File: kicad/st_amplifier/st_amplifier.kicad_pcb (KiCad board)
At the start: 2 copper layers, 170 x 90 mm, 71 parts

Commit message: Adding board st_amplifier.
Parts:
- moved DA1 113.8 mm to (148.6, 120.7)
- moved C1 109.8 mm to (128.9, 120.0), turned to 90 degrees
- moved C2 108.8 mm to (156.8, 119.4)
- moved C3 107.3 mm to (162.6, 120.7)
- moved R5 104.8 mm to (102.2, 74.9)
- moved XS2 102.4 mm to (111.8, 124.5)
- moved R10 99.3 mm to (106.7, 101.6)
- moved VD1 97.5 mm to (111.8, 105.4)
- moved C5 96.7 mm to (156.8, 104.8)
- moved R7 96.7 mm to (104.1, 109.2)
- moved R16 96.3 mm to (189.2, 124.5), turned to 0 degrees
- moved C13 96.0 mm to (177.2, 97.2)
- moved R8 95.7 mm to (177.2, 101.6)
- moved C4 95.7 mm to (128.9, 104.1)
- moved R13 95.6 mm to (221.0, 79.4), turned to 90 degrees
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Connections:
- DA5 pad 5: (no net) -> /CLIP_2
- XS2 pad 4: /CLIP_1 -> /CLIP_2
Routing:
- net /+29V: track 0.00 -> 305.4 mm, vias 0 -> 2
- net /-29V: track 0.00 -> 302.8 mm, vias 0 -> 3
- net /GND: track 0.00 -> 235.1 mm
- net /MUTE: track 0.00 -> 207.6 mm, vias 0 -> 2
- net /STBY: track 0.00 -> 158.8 mm, vias 0 -> 6
- net /CLIP_2: track 0.00 -> 146.0 mm, vias 0 -> 4
- net N-000003: track 0.00 -> 86.0 mm
- net /CLIP_1: track 0.00 -> 75.6 mm, vias 0 -> 2
- net N-0000035: track 0.00 -> 67.6 mm
- net /-15V: track 0.00 -> 59.3 mm
- net N-0000030: track 0.00 -> 54.4 mm
- net N-0000017: track 0.00 -> 47.6 mm
- net N-0000011: track 0.00 -> 46.2 mm
- net N-0000027: track 0.00 -> 44.5 mm
- net N-0000025: track 0.00 -> 39.9 mm
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- added copper zone on B.Cu, net /GND
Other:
- board size 170 x 90 mm -> 170 x 80 mm
- rule trace_min: 0.254 -> 0.25
- board text added: "+VCC"
- board text added: "-VCC"
- board text added: "CLIP 1"
- board text added: "CLIP 2"
- board text added: "GND"
- board text added: "IN 1"
- board text added: "IN 2"
- board text added: "OUT 1"
- board text added: "OUT 2"
- board text added: "SB"

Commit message: New commit.
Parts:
- moved R11 23.1 mm to (82.5, 105.4)
- moved R7 21.6 mm to (82.5, 109.2)
- moved VD1 18.8 mm to (93.3, 109.2), turned to 0 degrees
- moved R9 16.8 mm to (100.3, 105.4), turned to 0 degrees
- moved C18 8.62 mm to (103.5, 94.6)
- moved R10 7.43 mm to (109.2, 94.6), turned to 90 degrees
- moved C6 6.87 mm to (158.8, 109.2), turned to 0 degrees
- moved C3 6.35 mm to (158.8, 115.6), turned to 180 degrees
- moved C19 5.44 mm to (102.9, 100.3), turned to 180 degrees
- moved C11 3.56 mm to (118.4, 74.9)
- moved C2 2.69 mm to (158.8, 121.3)
- moved C5 2.29 mm to (158.8, 103.5)
- moved XS2 1.27 mm to (111.8, 125.7)
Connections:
- XS1 pad 1: /+29V -> /-29V
- XS1 pad 2: /GND -> /+29V
- XS1 pad 3: /-29V -> /GND
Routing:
- net /CLIP_2: track 146.0 -> 180.0 mm, vias 4 -> 2
- net /MU/ST: track 19.7 -> 45.4 mm
- net /MUTE: track 207.6 -> 227.8 mm, vias 2 -> 4
- net /STBY: track 158.8 -> 177.0 mm, vias 6 -> 5
- net /GND: track 235.1 -> 219.4 mm
- net /-29V: track 302.8 -> 316.9 mm
- net /+29V: track 305.4 -> 314.7 mm
- net /-15V: track 59.3 -> 63.4 mm
- net N-0000028: track 14.0 -> 11.4 mm
- net /+15V: track 34.6 -> 36.5 mm
- net N-0000011: track 46.2 -> 44.4 mm
- net N-0000012: track 13.9 -> 12.2 mm
- net N-0000026: track 27.4 -> 28.8 mm
- net N-0000025: track 39.9 -> 38.4 mm
- net /CLIP_1: track 75.6 -> 74.2 mm
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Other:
- net class Default: clearance 0.254 -> 0.35; trace_width 0.254 -> 0.5
- rule trace_clearance: 0.254 -> 0.35
- rule trace_min: 0.25 -> 0.35

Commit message: New commit.
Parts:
- added R21: 220, RESISTOR_0.25W, F.Cu at (200.0, 99.1)
- added R22: 220, RESISTOR_0.25W, F.Cu at (198.8, 114.9)
- moved C21 8.64 mm to (196.2, 95.2), turned to 0 degrees
- moved R12 5.24 mm to (200.0, 103.5), turned to 0 degrees
- moved C27 4.58 mm to (194.9, 112.4)
- moved R16 4.02 mm to (185.4, 125.7)
- moved R6 4.02 mm to (185.4, 120.0)
- moved C23 1.27 mm to (190.5, 102.9)
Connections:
- C20 pad 2: N-0000034 (its old number) -> N-0000033
- C21 pad 2: N-0000034 (its old number) -> N-0000032
- C24 pad 2: N-000001 -> N-000002
- C27 pad 2: N-000001 -> N-000003
- DA3 pad 3: N-0000034 (its old number) -> N-0000032
- DA3 pad 5: N-000001 -> N-000003
- R12 pad 2: N-0000034 (its old number) -> N-0000033
- R18 pad 2: N-000001 -> N-000002
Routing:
- net N-0000034 (its old number): track 37.7 -> 0.00 mm
- net N-000001: track 28.5 -> 0.00 mm
- net N-0000032: track 0.00 -> 25.2 mm
- net N-000003: track 0.00 -> 18.4 mm
- net N-000002: track 0.00 -> 17.2 mm
- net N-0000033: track 0.00 -> 10.8 mm
- net N-000004: track 26.7 -> 23.8 mm
- net N-0000016: track 48.1 -> 50.9 mm
- net /-15V: track 63.4 -> 62.9 mm

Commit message: New commit.
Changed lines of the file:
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@@
     (area 67.9506 45.9796 241.9294 131.4394)
     (thickness 1.6002)
-    (drawings 30)
+    (drawings 28)
     (tracks 440)
     (zones 0)
@@
       (drillshape 0)
       (scaleselection 1)
-      (outputdirectory ../../../../Документы/GERBER_st_amplifier/))
+      (outputdirectory "/home/vdn/Рабочий стол/st_amplifier_doc/"))
   )
   (net 0 "")
@@
     (effects (font (size 1.7 1.5) (thickness 0.3)))
   )
-  (gr_line (start 135.255 125.73) (end 146.05 125.73) (angle 90) (layer F.SilkS) (width 0.381))
-  (gr_line (start 135.255 115.57) (end 146.05 115.57) (angle 90) (layer F.SilkS) (width 0.381))
   (gr_text GND (at 231.775 111.125) (layer F.SilkS)
     (effects (font (size 1.27 1) (thickness 0.25)))

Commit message: New commit.
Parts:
- removed R21, R22: 220, RESISTOR_0.25W
- added 1_PIN: P***, 1_pin, F.Cu at (145.0, 105.0)
- added 1_PIN: P***, 1_pin, F.Cu at (142.6, 122.2)
- moved C21 3.42 mm to (197.5, 98.4), turned to 180 degrees
- moved R18 3.18 mm to (200.7, 115.6), turned to 270 degrees
- moved R12 0.90 mm to (200.7, 102.9), turned to 180 degrees
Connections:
- C20 pad 2: N-0000033 -> N-0000034
- C21 pad 2: N-0000032 (its old number) -> N-0000034
- C24 pad 2: N-000002 (its old number) -> N-000001
- C27 pad 2: N-000003 (its old number) -> N-000001
- DA3 pad 3: N-0000032 (its old number) -> N-0000034
- DA3 pad 5: N-000003 (its old number) -> N-000001
- R12 pad 2: N-0000033 -> N-0000034
- R18 pad 2: N-000002 (its old number) -> N-000001
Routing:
- net N-0000034: track 0.00 -> 37.5 mm
- net N-000001: track 0.00 -> 27.0 mm
- net N-0000032 (its old number): track 25.2 -> 0.00 mm
- net N-000003 (its old number): track 18.4 -> 0.00 mm
- net N-000002 (its old number): track 17.2 -> 0.00 mm
- net N-0000033: track 10.8 -> 0.00 mm
- net N-0000017: track 50.9 -> 51.9 mm

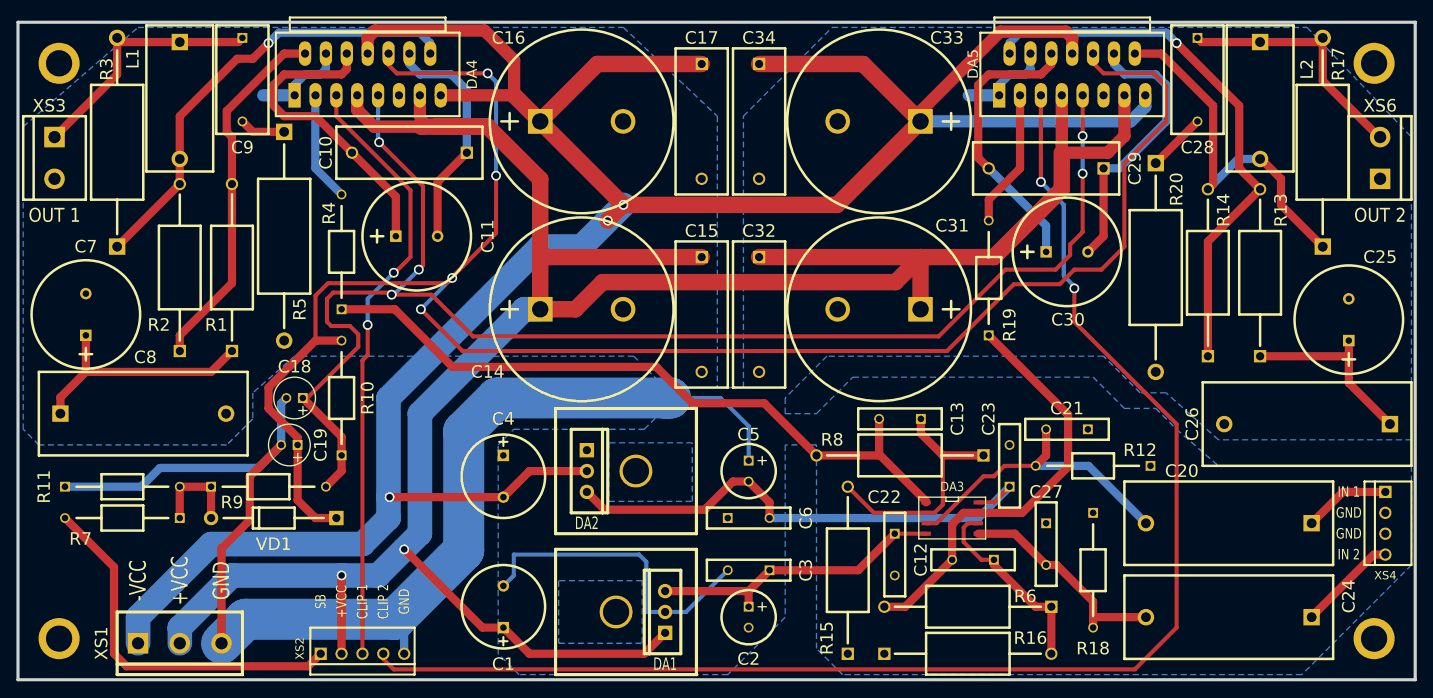
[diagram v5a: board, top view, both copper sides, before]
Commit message: Completely threw PCB board st_amplifier.
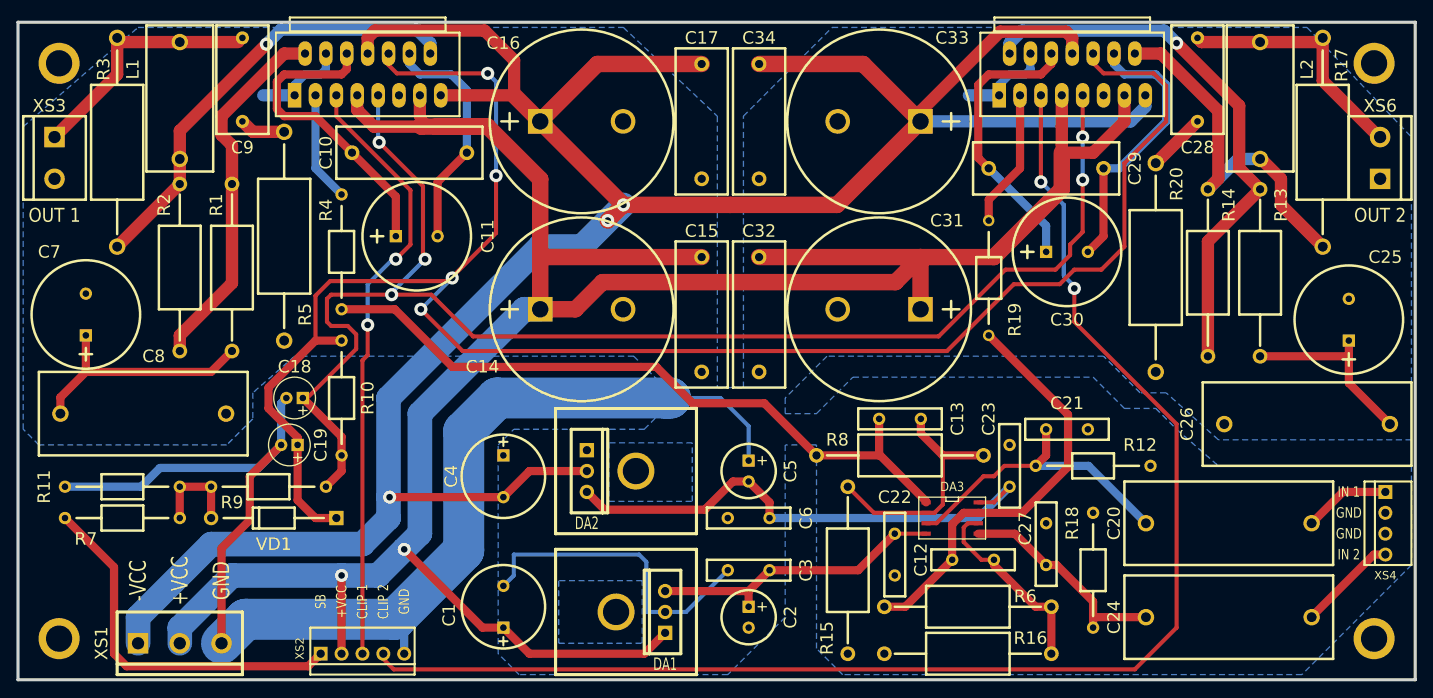
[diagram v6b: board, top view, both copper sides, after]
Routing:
- net /+29V: track 314.6 -> 313.5 mm
- net N-0000030: track 55.5 -> 54.8 mm
- net N-0000036: track 30.7 -> 31.4 mm
- net N-0000011: track 44.4 -> 44.9 mm
- net N-0000027: track 44.5 -> 45.0 mm
- net /STBY: track 177.0 -> 176.5 mm

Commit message: Fixed errors.
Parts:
- R1: value 1 к +/-0.5% -> 2 к +/-0.5%
- R13: value 1 к +/- 0.5% -> 2 к +/-0.5%
- R14: value 2 к +/- 0.5% -> 28.7 к +/-0.5%
- R19, R4: value 2,7 к -> 100
- R2: value 2 к +/-0.5% -> 28.7 к +/-0.5%
- R6, R8: value 47 к +/-0.5% -> 22.1 к +/-0.5%
- moved C33 0.13 mm to (174.5, 61.0), turned to 0 degrees
- turned C16 to 180 degrees
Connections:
- C16 pad 1: /-29V -> /GND
- C16 pad 2: /GND -> /-29V
- C22 pad 1: /+15V -> /-15V
- C23 pad 1: /-15V -> /+15V
- C33 pad 1: /-29V -> /GND
- C33 pad 2: /GND -> /-29V
- DA3 pad 4: /+15V -> /-15V
- DA3 pad 8: /-15V -> /+15V
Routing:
- net /+15V: track 36.5 -> 53.7 mm
- net /-15V: track 62.9 -> 47.3 mm

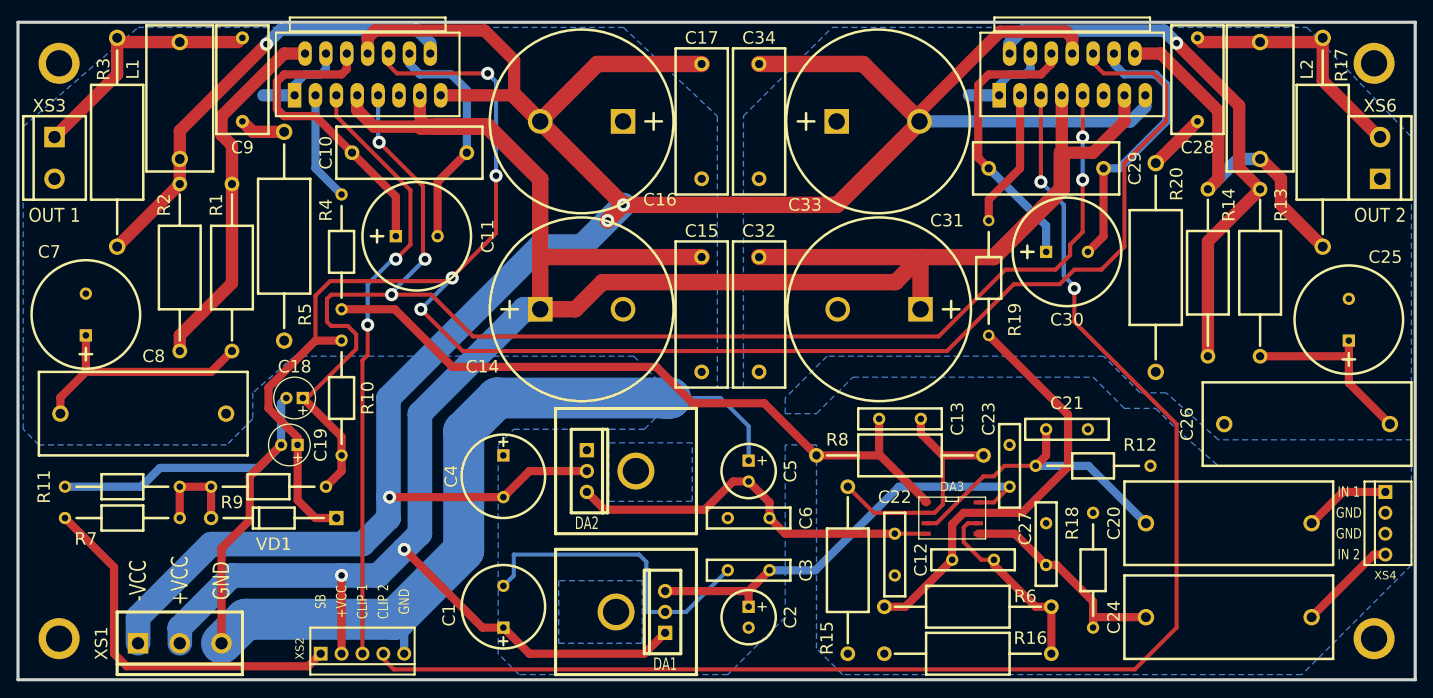
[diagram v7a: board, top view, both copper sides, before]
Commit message: Adding new version st_amplifier.
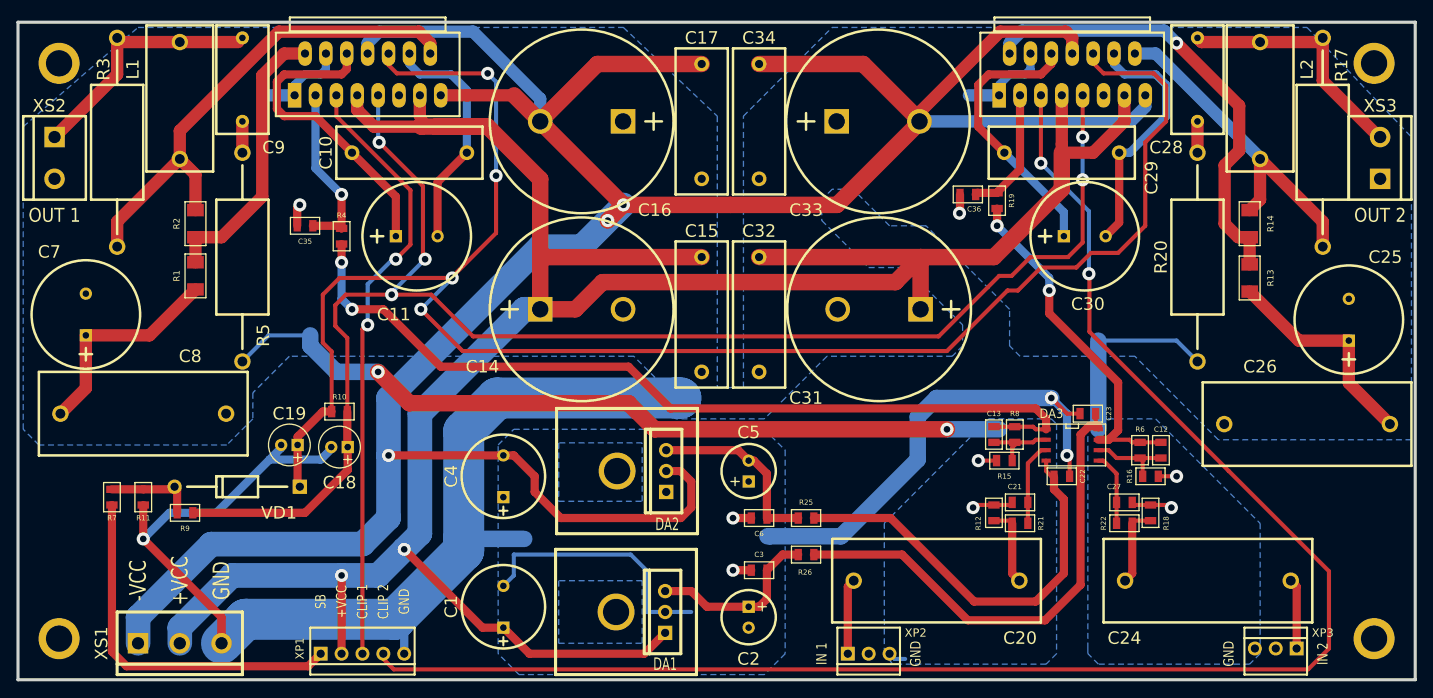
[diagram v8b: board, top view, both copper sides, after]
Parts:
- removed XS4: WF-4, WF-4
- added C35: 22 п, SMD0805, F.Cu at (104.8, 73.7)
- added C36: 22 п, SMD0805, F.Cu at (185.4, 69.8)
- added R21: 220, SMD0805, F.Cu at (191.8, 109.9)
- added R22: 220, SMD0805, F.Cu at (204.5, 109.9)
- added R25: 4.7, SMD0805, F.Cu at (165.7, 109.2)
- added R26: 4.7, SMD0805, F.Cu at (165.7, 113.7)
- added XP2: WF-3, WF-3, F.Cu at (173.4, 125.7)
- added XP3: WF-3, WF-3, F.Cu at (222.9, 125.1)
- C12, C13: value 10 п -> 22 п; footprint CAPACITOR_K10-17 -> SMD0805
- C21, C27: value 100 п -> 220 п; footprint CAPACITOR_K10-17 -> SMD0805
- C22, C23, C3, C6: footprint CAPACITOR_K10-17 -> SMD0805
- C28, C9: value 0.1 мк -> 0.047 мк
- R1: value 2 к +/-0.5% -> 2 к +/-0.5%; footprint RESISTOR_1W -> SMD1206
- R10, R11, R12, R18, R19, R4, R7, R9: footprint RESISTOR_0.25W -> SMD0805
- R13, R14: footprint RESISTOR_1W -> SMD1206
- R15, R16, R6, R8: footprint RESISTOR_1W -> SMD0805
- R2: value 28.7 к +/-0.5% -> 28.7 к +/-0.5%; footprint RESISTOR_1W -> SMD1206
- moved C20 36.2 mm to (181.6, 116.8), turned to 0 degrees
- moved R16 31.0 mm to (207.6, 104.1), turned to 180 degrees
- moved R6 28.3 mm to (206.4, 101.0), turned to 90 degrees
- moved C12 26.5 mm to (208.9, 101.0), turned to 90 degrees
- moved R15 23.3 mm to (189.9, 102.2), turned to 0 degrees
- moved C22 22.4 mm to (196.8, 104.1), turned to 0 degrees
- moved DA3 17.1 mm to (198.1, 100.3)
- moved R8 14.2 mm to (191.1, 99.1), turned to 90 degrees
- moved R12 13.4 mm to (188.6, 108.6), turned to 270 degrees
- moved C13 11.6 mm to (188.6, 99.1), turned to 90 degrees
- moved C23 11.4 mm to (200.0, 96.5), turned to 180 degrees
- moved C27 10.8 mm to (204.5, 107.3), turned to 180 degrees
- moved R9 10.6 mm to (90.2, 108.6)
- moved C21 10.6 mm to (191.8, 107.3), turned to 0 degrees
- moved R18 9.88 mm to (207.6, 108.6)
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- renumbered XS2 to XP1, XS3 to XS2, XS6 to XS3
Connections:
- C20 pad 2: N-0000031 -> N-0000033
- C21 pad 2: N-0000031 -> N-0000032
- C22 pad 1: /-15V -> N-0000019
- C23 pad 1: /+15V -> N-0000018
- C24 pad 2: N-000002 -> N-000001
- C27 pad 2: N-000002 -> N-000004
- DA3 pad 3: N-0000031 -> N-0000032
- DA3 pad 4: /-15V -> N-0000019
- DA3 pad 5: N-000002 -> N-000004
- DA3 pad 8: /+15V -> N-0000018
- R12 pad 2: N-0000031 -> N-0000033
- R18 pad 2: N-000002 -> N-000001
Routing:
- net /GND: track 219.4 -> 403.2 mm, vias 0 -> 13
- net N-0000018: track 0.00 -> 60.8 mm
- net N-0000019: track 0.00 -> 50.8 mm
- net N-0000031: track 37.5 -> 0.00 mm
- net /+15V: track 53.7 -> 21.7 mm
- net N-000002: track 27.0 -> 0.00 mm
- net /-29V: track 316.9 -> 342.9 mm
- net /-15V: track 47.3 -> 22.6 mm
- net N-0000020: track 29.8 -> 8.84 mm
- net N-000005: track 85.4 -> 106.2 mm, vias 0 -> 2
- net /CLIP_2: track 180.0 -> 199.1 mm
- net N-000006: track 23.8 -> 10.4 mm
- net /MUTE: track 227.8 -> 215.5 mm
- net N-0000034: track 67.8 -> 55.8 mm
- net N-0000025: track 45.0 -> 34.3 mm
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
